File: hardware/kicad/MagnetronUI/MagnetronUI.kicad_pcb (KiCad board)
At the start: 4 copper layers, 119.1 x 47.5 mm, 60 parts, among them J1 Conn_01x04, J2 Conn_02x13_Counter_Clockwise, SW1 SW_Push, SW2 SW_Push, SW3 RotaryEncoder_Switch_MP, SW4 RotaryEncoder_Switch_MP, SW5 RotaryEncoder_Switch_MP, SW6 RotaryEncoder_Switch_MP, SW7 RotaryEncoder_Switch_MP

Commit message: feat: break into multiple boards
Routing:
- net GND: vias 17 -> 39
- added copper zone on B.Cu, net GND
- added copper zone on F.Cu, net GND
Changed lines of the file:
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@@
+	)
+	(via
+		(at 104.14 93.726)
+		(size 0.6)
+		(drill 0.3)
+		(layers "F.Cu" "B.Cu")
+		(net 2)
 	)
 	(via
@@
 	)
 	(via
+		(at 88.646 107.95)
+		(size 0.6)
+		(drill 0.3)
+		(layers "F.Cu" "B.Cu")
+		(net 2)
+	)
+	(via
 		(at 105.1055 120.7005)
 		(size 0.6)
@@
 	)
 	(via
+		(at 123.950606 107.711601)
+		(size 0.6)
+		(drill 0.3)
+		(layers "F.Cu" "B.Cu")
+		(net 2)
+	)
+	(via
 		(at 70.8155 120.9545)
 		(size 0.6)
@@
 	)
 	(via
+		(at 108.204 107.95)
+		(size 0.6)
+		(drill 0.3)
+		(layers "F.Cu" "B.Cu")
+		(net 2)
+	)
+	(via
+		(at 131.826 87.63)
+		(size 0.6)
+		(drill 0.3)
+		(layers "F.Cu" "B.Cu")
+		(net 2)
+	)
+	(via
 		(at 149.62725 118.1605)
 		(size 0.6)
@@
 	)
 	(via
+		(at 64.516 92.71)
+		(size 0.6)
+		(drill 0.3)
+		(layers "F.Cu" "B.Cu")
+		(net 2)
+	)
+	(via
+		(at 72.055979 94.517848)
+		(size 0.6)
+		(drill 0.3)
+		(layers "F.Cu" "B.Cu")
+		(net 2)
+	)
+	(via
 		(at 103.5815 102.17975)
 		(size 0.6)
@@
 	)
 	(via
+		(at 75.184 82.296)
+		(size 0.6)
+		(drill 0.3)
+		(layers "F.Cu" "B.Cu")
+		(net 2)
+	)
+	(via
+		(at 55.372 107.95)
+		(size 0.6)
+		(drill 0.3)
+		(layers "F.Cu" "B.Cu")
+		(net 2)
+	)
+	(via
+		(at 86.106 96.266)
+		(size 0.6)
+		(drill 0.3)
+		(layers "F.Cu" "B.Cu")
+		(net 2)
+	)
+	(via
+		(at 112.014 95.504)
+		(size 0.6)
+		(drill 0.3)
+		(layers "F.Cu" "B.Cu")
+		(net 2)
+	)
+	(via
 		(at 164.66375 118.1605)
 		(size 0.6)
@@
 	)
 	(via
+		(at 109.728 100.838)
+		(size 0.6)
+		(drill 0.3)
+		(layers "F.Cu" "B.Cu")
+		(net 2)
+	)
+	(via
+		(at 132.08 97.028)
+		(size 0.6)
+		(drill 0.3)
+		(layers "F.Cu" "B.Cu")
+		(net 2)
+	)
+	(via
+		(at 104.14 88.646)
+		(size 0.6)
+		(drill 0.3)
+		(layers "F.Cu" "B.Cu")
+		(net 2)
+	)
+	(via
+		(at 75.438 100.838)
+		(size 0.6)
+		(drill 0.3)
+		(layers "F.Cu" "B.Cu")
+		(net 2)
+	)
+	(via
+		(at 72.136 107.95)
+		(size 0.6)
+		(drill 0.3)
+		(layers "F.Cu" "B.Cu")
+		(net 2)
+	)
+	(via
+		(at 58.674 100.838)
+		(size 0.6)
+		(drill 0.3)
+		(layers "F.Cu" "B.Cu")
+		(net 2)
+	)
+	(via
+		(at 92.456 100.838)
+		(size 0.6)
+		(drill 0.3)
+		(layers "F.Cu" "B.Cu")
+		(net 2)
+	)
+	(via
 		(at 64.2115 102.17975)
 		(size 0.6)
@@
 	)
 	(via
+		(at 81.28 93.98)
+		(size 0.6)
+		(drill 0.3)
+		(layers "F.Cu" "B.Cu")
+		(net 2)
+	)
+	(via
 		(at 87.8335 120.1925)
 		(size 0.6)
@@
 	)
 	(via
+		(at 126.492 100.838)
+		(size 0.6)
+		(drill 0.3)
+		(layers "F.Cu" "B.Cu")
+		(net 2)
+	)
+	(via
 		(at 53.5435 120.9545)
+		(size 0.6)
+		(drill 0.3)
+		(layers "F.Cu" "B.Cu")
+		(net 2)
+	)
+	(via
+		(at 80.772 86.36)
+		(size 0.6)
+		(drill 0.3)
+		(layers "F.Cu" "B.Cu")
+		(net 2)
+	)
+	(via
+		(at 92.202 93.726)
 		(size 0.6)
 		(drill 0.3)
@@
 		(net 2)
 		(net_name "GND")
-		(layer "In1.Cu")
+		(layers "F.Cu" "B.Cu" "In1.Cu")
 		(hatch edge 0.5)
 		(priority 3)
@@
 		(filled_areas_thickness no)
 		(fill yes
-			(thermal_gap 0.5)
+			(thermal_gap 0.25)
 			(thermal_bridge_width 0.5)
 		)

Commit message: chore: cleanup
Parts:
- moved SW1 20.5 mm to (161.0, 115.6), turned to -90 degrees
- moved R4 18.4 mm to (153.7, 99.8), turned to -90 degrees
- moved R2 15.1 mm to (153.7, 103.9), turned to 90 degrees
- moved R3 14.8 mm to (153.7, 114.0), turned to 90 degrees
- moved C2 13.6 mm to (153.7, 107.9), turned to -90 degrees
- moved SW2 10.7 mm to (161.0, 101.3), turned to -90 degrees
- moved R1 10.2 mm to (153.7, 118.0), turned to -90 degrees
- moved C1 7.26 mm to (153.7, 122.1), turned to -90 degrees
- moved J2 5.79 mm to (115.6, 81.5)
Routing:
- net /aux1_btn: track 48.9 -> 33.8 mm
- net /volume_encoder_a: track 41.6 -> 33.7 mm
- net /aux2_btn: track 37.3 -> 44.4 mm
- net /encoder_aux1_b: track 39.9 -> 33.7 mm
- net /volume_encoder_b: track 53.1 -> 47.2 mm
- net /menu_encoder_a: track 65.2 -> 59.4 mm
- net /sda: track 13.2 -> 19.0 mm
- net /speed_encoder_b: track 63.0 -> 57.2 mm
- net /speed_encoder_a: track 54.1 -> 48.3 mm
- net /menu_encoder_btn: track 87.2 -> 81.4 mm
- net /menu_encoder_b: track 79.7 -> 73.9 mm
- net /scl: track 9.04 -> 14.8 mm
- net /encoder_aux1_btn: track 60.3 -> 54.6 mm
- net /encoder_aux1_a: track 31.6 -> 25.9 mm
- net /volume_encoder_btn: track 63.3 -> 57.8 mm
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
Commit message: feat: cleanup
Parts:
- removed C1, C2: C, Capacitor_SMD:C_0805_2012Metric_Pad1.18x1.45mm_HandSolder
- removed C10, C11, C12, C13, C14, C15, C16, C17, C3, C4, C5, C6, C7, C8, C9: .01uf, Capacitor_SMD:C_0805_2012Metric_Pad1.18x1.45mm_HandSolder
- removed R1, R2, R3, R4: R, Resistor_SMD:R_0805_2012Metric_Pad1.20x1.40mm_HandSolder
- removed R10, R11, R13, R15, R16, R17, R19, R21, R22, R23, R25, R27, R28, R29, R31, R33, R34, R5, R7, R9: 10k, Resistor_SMD:R_0805_2012Metric_Pad1.20x1.40mm_HandSolder
- moved SW2 3.34 mm to (160.8, 104.6)
- moved SW1 1.33 mm to (160.8, 116.9)
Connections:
- R12 pad 2: Net-(R11-Pad1) -> /encoder_aux2_a
- R14 pad 1: Net-(R14-Pad1) -> /encoder_aux2_b
- R18 pad 2: Net-(R17-Pad1) -> /menu_encoder_a
- R20 pad 1: Net-(R20-Pad1) -> /menu_encoder_b
- R24 pad 2: Net-(R23-Pad1) -> /speed_encoder_a
- R26 pad 1: Net-(R26-Pad1) -> /speed_encoder_b
- R30 pad 2: Net-(R29-Pad1) -> /volume_encoder_a
- R32 pad 1: Net-(R32-Pad1) -> /volume_encoder_b
- R6 pad 2: Net-(R5-Pad1) -> /encoder_aux1_a
- R8 pad 1: Net-(R10-Pad1) -> /encoder_aux1_b
- SW1 pad 1: Net-(R1-Pad1) -> /aux2_btn
- SW2 pad 1: Net-(R2-Pad2) -> /aux1_btn
- SW3 pad A: Net-(R5-Pad1) -> /encoder_aux1_a
- SW3 pad B: Net-(R10-Pad1) -> /encoder_aux1_b
- SW3 pad S2: Net-(R7-Pad1) -> /encoder_aux1_btn
- SW4 pad A: Net-(R11-Pad1) -> /encoder_aux2_a
- SW4 pad B: Net-(R14-Pad1) -> /encoder_aux2_b
- SW4 pad S2: Net-(R13-Pad1) -> /encoder_aux2_btn
- SW5 pad A: Net-(R17-Pad1) -> /menu_encoder_a
- SW5 pad B: Net-(R20-Pad1) -> /menu_encoder_b
- SW5 pad S2: Net-(R19-Pad1) -> /menu_encoder_btn
- SW6 pad A: Net-(R23-Pad1) -> /speed_encoder_a
- SW6 pad B: Net-(R26-Pad1) -> /speed_encoder_b
- SW6 pad S2: Net-(R25-Pad1) -> /speed_encoder_btn
- SW7 pad A: Net-(R29-Pad1) -> /volume_encoder_a
- SW7 pad B: Net-(R32-Pad1) -> /volume_encoder_b
- SW7 pad S2: Net-(R31-Pad1) -> /volume_encoder_btn
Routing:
- net GND: track 23.1 -> 0.00 mm, vias 40 -> 0
- net /encoder_aux2_btn: track 49.4 -> 36.9 mm
- net /speed_encoder_btn: track 79.3 -> 69.1 mm, vias 2 -> 0
- net Net-(R2-Pad2): track 9.62 -> 0.00 mm
- net /encoder_aux1_btn: track 54.6 -> 45.8 mm, vias 1 -> 0
- net Net-(R1-Pad1): track 8.76 -> 0.00 mm
- net /speed_encoder_a: track 48.3 -> 55.8 mm, vias 0 -> 1
- net Net-(R13-Pad1): track 6.58 -> 0.00 mm
- net Net-(R19-Pad1): track 6.58 -> 0.00 mm
- net Net-(R7-Pad1): track 6.58 -> 0.00 mm
- net Net-(R31-Pad1): track 6.58 -> 0.00 mm
- net Net-(R25-Pad1): track 6.58 -> 0.00 mm
- net /encoder_aux2_b: track 33.8 -> 27.4 mm
- net /menu_encoder_a: track 59.4 -> 65.7 mm, vias 1 -> 0
- net Net-(R32-Pad1): track 6.13 -> 0.00 mm
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
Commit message: feat: updates
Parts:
- removed the SW2 at (160.8, 104.6)
- renumbered R18 to R1, R14 to R10, R20 to R2, R24 to R3, R26 to R4, R30 to R5, R32 to R6, R6 to R7, R12 to R9, SW5 to SW2, SW6 to SW3, SW7 to SW4, SW3 to SW5, SW4 to SW6
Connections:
- J1 pad 2: +3.3V -> +5V
- J2 pad 17: /aux1_btn -> unconnected-(J2-Pin_17-Pad17)
- J2 pad 18: /aux2_btn -> /aux1_btn
- J2 pad 22: unconnected-(J2-Pin_22-Pad22) -> +5V
- SW1 pad 1: /aux2_btn -> /aux1_btn
- SW5 pad S2: /encoder_aux1_btn -> /encoder_aux1/encoder_btn
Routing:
- net /aux2_btn: track 46.1 -> 0.00 mm
- net +5V: track 0.00 -> 21.5 mm
- net /aux1_btn: track 36.5 -> 46.1 mm

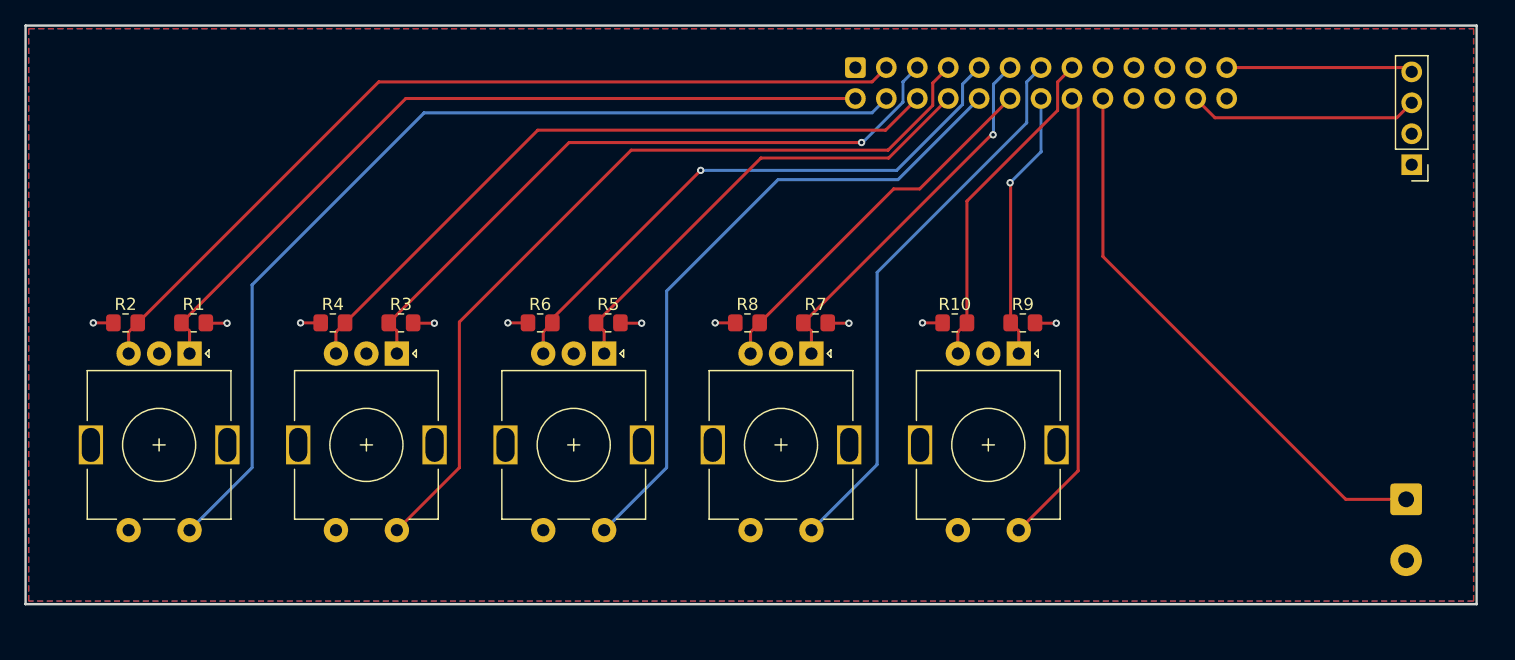
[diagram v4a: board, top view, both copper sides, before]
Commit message: feat: update to 2 layer board
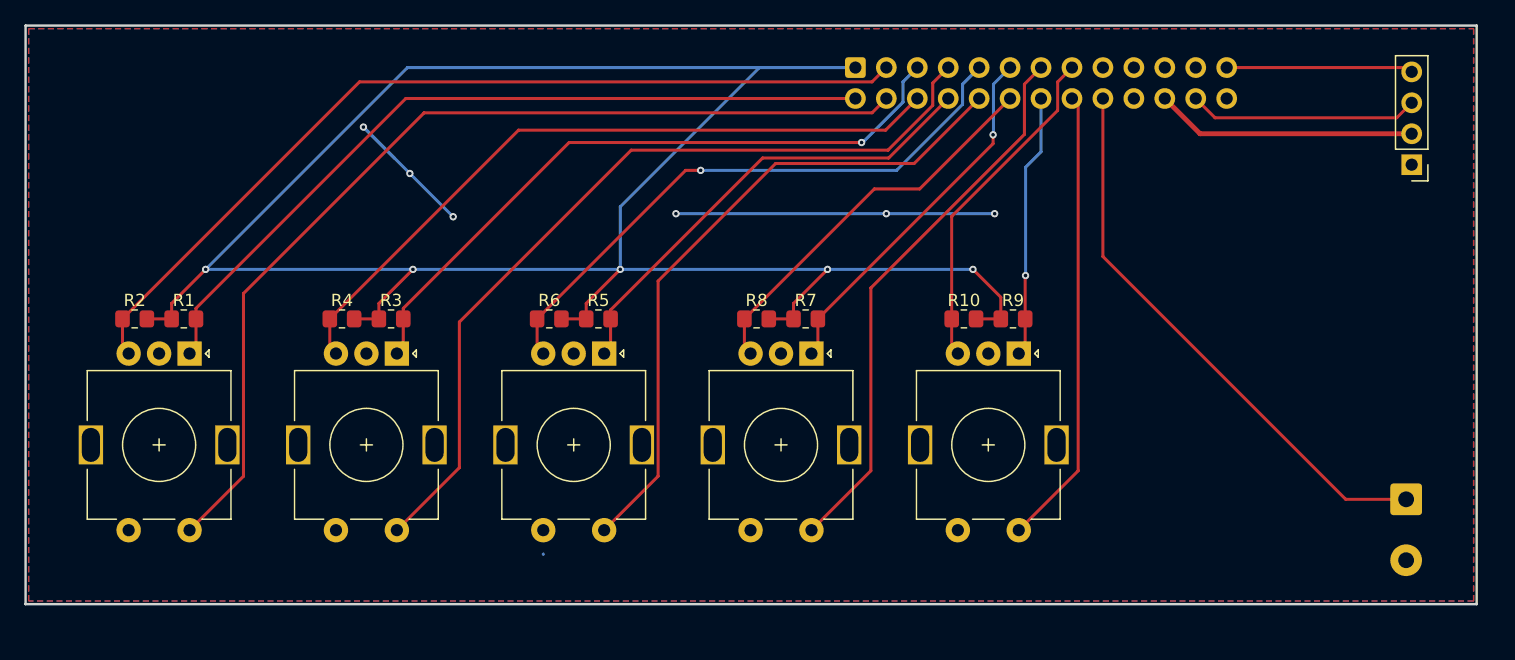
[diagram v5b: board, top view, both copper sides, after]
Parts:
- moved R3 0.87 mm to (77.5, 102.1), turned to 0 degrees
- moved R5 0.87 mm to (94.5, 102.1), turned to 0 degrees
- moved R7 0.87 mm to (111.5, 102.1), turned to 0 degrees
- moved R1 0.87 mm to (60.4, 102.1), turned to 0 degrees
- moved R9 0.87 mm to (128.5, 102.1), turned to 0 degrees
- moved R2 0.82 mm to (56.4, 102.1), turned to 0 degrees
- moved R10 0.82 mm to (124.5, 102.1), turned to 0 degrees
- moved R4 0.82 mm to (73.4, 102.1), turned to 0 degrees
- moved R6 0.82 mm to (90.4, 102.1), turned to 0 degrees
- moved R8 0.82 mm to (107.5, 102.1), turned to 0 degrees
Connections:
- SW5 pad S2: /encoder_aux1/encoder_btn -> /encoder_aux1_btn
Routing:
- net +3.3V: track 16.5 -> 180.6 mm, vias 10 -> 5
- net GND: track 0.00 -> 40.2 mm, vias 0 -> 6
- net /encoder_aux1_a: track 30.9 -> 29.5 mm
- net /volume_encoder_a: track 39.3 -> 38.0 mm
- net /encoder_aux2_a: track 22.3 -> 21.0 mm
- net /menu_encoder_a: track 65.7 -> 64.5 mm
- net /speed_encoder_a: track 55.8 -> 54.5 mm
- net /volume_encoder_btn: track 54.0 -> 54.8 mm
- net /volume_encoder_b: track 47.4 -> 48.1 mm
- net /menu_encoder_b: track 73.0 -> 73.6 mm
- net /encoder_aux1_b: track 31.0 -> 31.6 mm
- net /speed_encoder_b: track 57.4 -> 58.1 mm
- removed copper zone on In2.Cu, net +3.3V
- removed copper zone on In1.Cu, net GND
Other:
- copper layers 4 -> 2

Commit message: chore: cleanup/mounting holes
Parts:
- added H1: MountingHole_Pad, MountingHole:MountingHole_3.2mm_M3_ISO7380_Pad_TopBottom, F.Cu at (51.6, 82.5)
- added H2: MountingHole_Pad, MountingHole:MountingHole_3.2mm_M3_ISO7380_Pad_TopBottom, F.Cu at (162.1, 82.3)
- added H3: MountingHole_Pad, MountingHole:MountingHole_3.2mm_M3_ISO7380_Pad_TopBottom, F.Cu at (161.8, 121.4)
- added H4: MountingHole_Pad, MountingHole:MountingHole_3.2mm_M3_ISO7380_Pad_TopBottom, F.Cu at (51.6, 123.5)
- moved J1 11.0 mm to (164.9, 99.8)
- moved SW1 8.44 mm to (161.3, 108.5)
- moved J2 4.05 mm to (119.4, 82.9)
- moved R10 4.05 mm to (128.3, 103.5)
- moved R3 4.05 mm to (81.3, 103.5)
- moved R4 4.05 mm to (77.2, 103.5)
- moved R5 4.05 mm to (98.3, 103.5)
- moved R6 4.05 mm to (94.2, 103.5)
- moved R7 4.05 mm to (115.3, 103.5)
- moved R8 4.05 mm to (111.3, 103.5)
- moved R9 4.05 mm to (132.3, 103.5)
- moved SW3 4.05 mm to (81.7, 106.3)
- moved SW4 4.05 mm to (98.8, 106.3)
- moved SW5 4.05 mm to (115.8, 106.3)
- moved SW6 4.05 mm to (132.8, 106.3)
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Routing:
- net /aux1_btn: track 46.1 -> 36.8 mm
- net /scl: track 14.8 -> 18.9 mm
- net +5V: track 21.5 -> 25.0 mm
- net /sda: track 18.9 -> 21.5 mm
- net +3.3V: track 180.6 -> 182.3 mm
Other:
- board size 119.1 x 47.5 mm -> 120 x 50 mm

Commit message: chore: cleanup
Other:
- board text added: "+5"
- board text added: "Display"
- board text added: "aux1 encoder"
- board text added: "aux2 encoder"
- board text added: "gnd"
- board text added: "lcd"
- board text added: "main"
- board text added: "menu"
- board text added: "scl"
- board text added: "sda"
- board text added: "speed"
- board text added: "volume"

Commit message: chore: cleanup
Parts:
- added Q1: BSS138, Package_TO_SOT_SMD:SOT-23, F.Cu at (154.7, 92.5)
- added Q2: BSS138, Package_TO_SOT_SMD:SOT-23, F.Cu at (154.7, 98.4)
- added R11: 10k, Resistor_SMD:R_0805_2012Metric_Pad1.20x1.40mm_HandSolder, F.Cu at (157.7, 92.5)
- added R12: 10k, Resistor_SMD:R_0805_2012Metric_Pad1.20x1.40mm_HandSolder, F.Cu at (151.6, 92.5)
- added R13: 10k, Resistor_SMD:R_0805_2012Metric_Pad1.20x1.40mm_HandSolder, F.Cu at (157.7, 98.3)
- added R14: 10k, Resistor_SMD:R_0805_2012Metric_Pad1.20x1.40mm_HandSolder, F.Cu at (151.6, 98.3)
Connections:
- J1 pad 3: /sda -> /sda_5v
- J1 pad 4: /scl -> /scl_5v
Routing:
- net +3.3V: track 182.3 -> 264.5 mm, vias 5 -> 7
- net +5V: track 25.0 -> 53.4 mm, vias 0 -> 1
- net /sda_5v: track 0.00 -> 10.8 mm
- net /scl_5v: track 0.00 -> 10.0 mm
- net /scl: track 18.9 -> 14.4 mm
- net /sda: track 21.5 -> 17.8 mm
- net GND: vias 6 -> 10
